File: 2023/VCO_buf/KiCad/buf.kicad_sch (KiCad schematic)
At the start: 8 parts, among them M1 PMOS_OR1, M2 NMOS_OR1, M3 PMOS_OR1, M4 NMOS_OR1, M5 PMOS_OR1, M6 NMOS_OR1, M7 PMOS_OR1, M8 NMOS_OR1

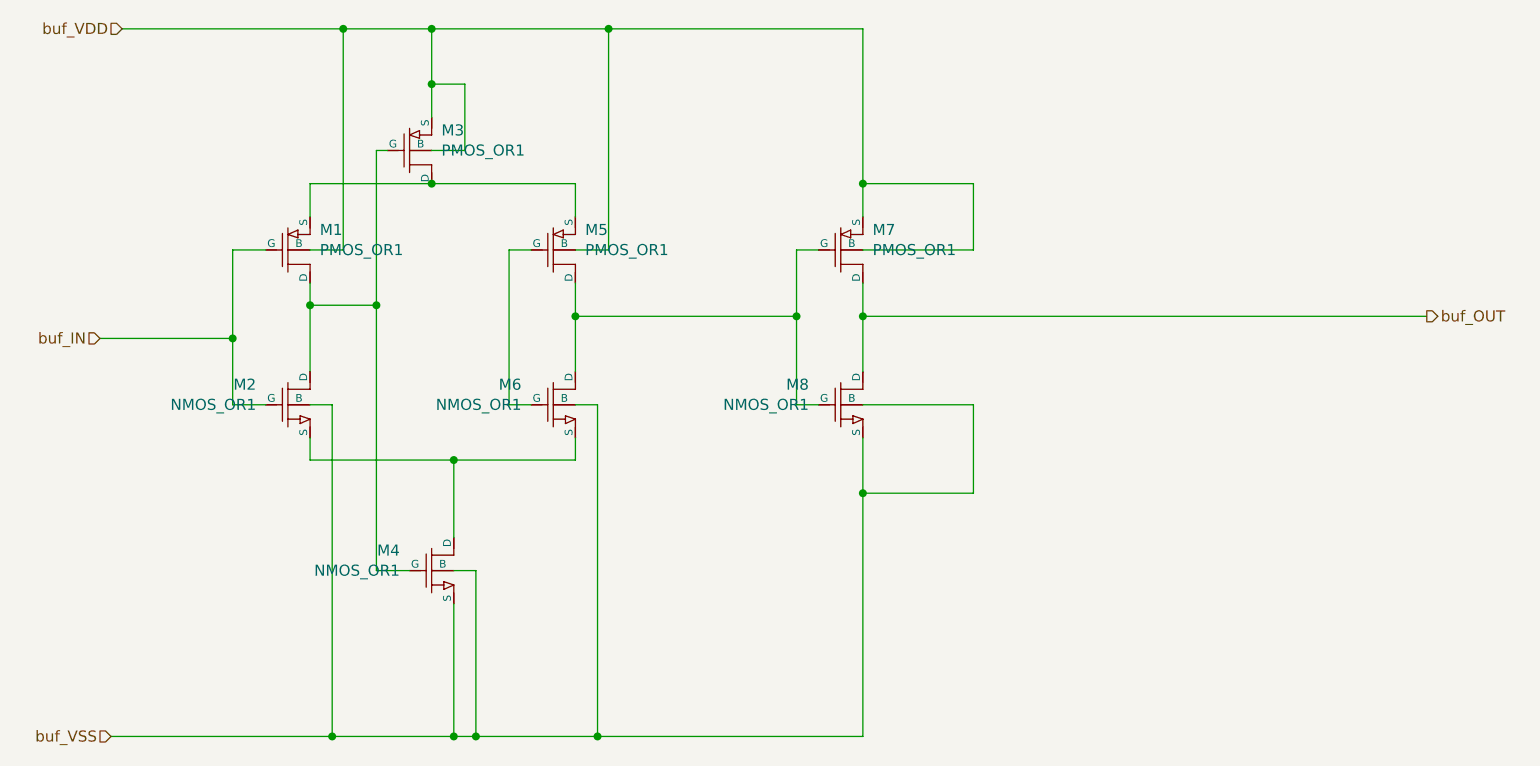
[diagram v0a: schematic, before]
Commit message: 最後に２つバッファつけて LVS OK.
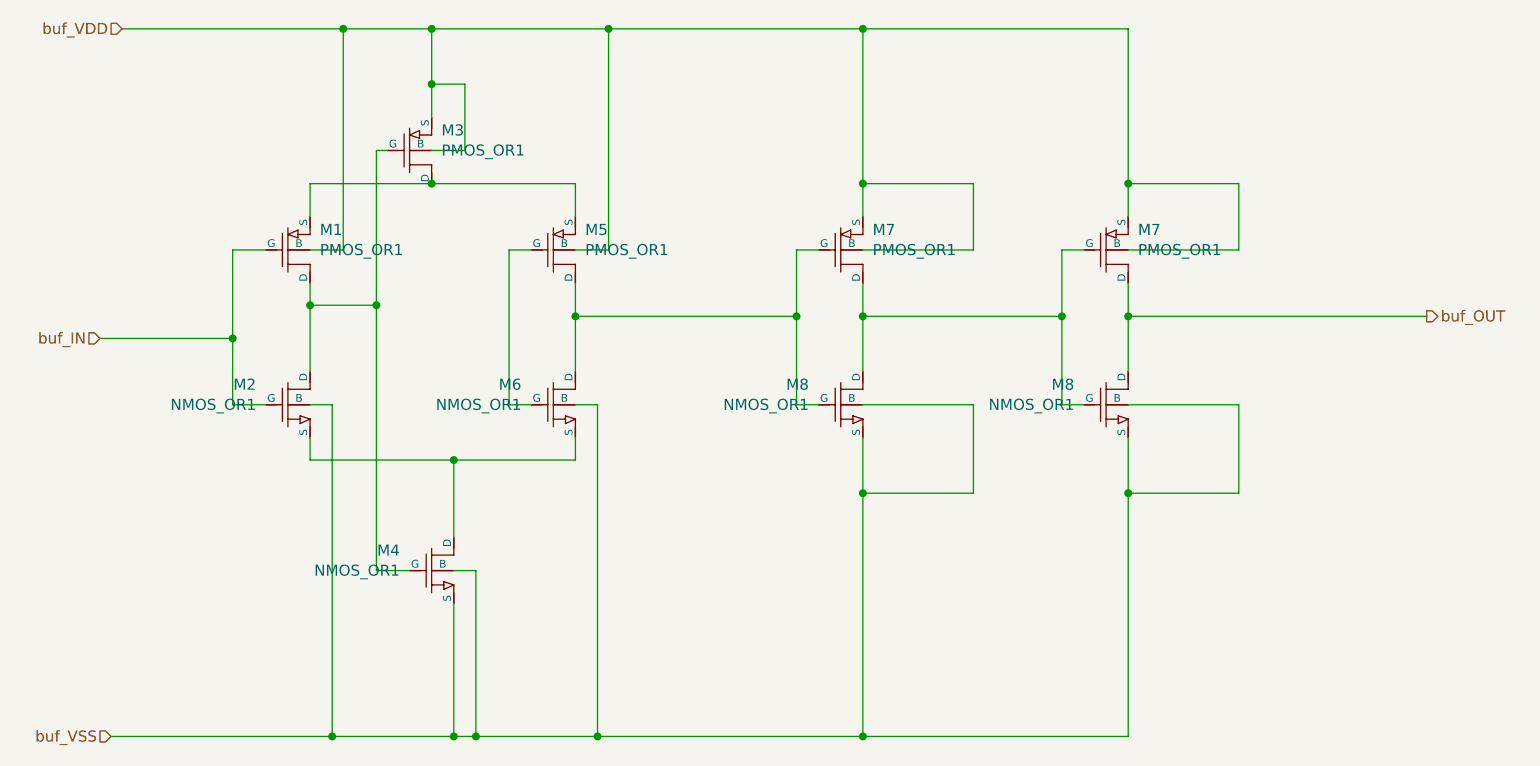
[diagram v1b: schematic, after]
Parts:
- added M7: PMOS_OR1, symbol 0_OR1Symbols:PMOS_OR1
- added M8: NMOS_OR1, symbol 0_OR1Symbols:NMOS_OR1
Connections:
- net buf_OUT: now also M7.1 (D), M8.1 (D); no longer M7.1 (D), M8.1 (D)
- net buf_VDD: now also M7.3 (S), M7.4 (B)
- net buf_VSS: now also M8.3 (S), M8.4 (B)
- new net: M7.1 (D), M7.2 (G), M8.1 (D), M8.2 (G)
